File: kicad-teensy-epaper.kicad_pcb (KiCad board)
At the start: 2 copper layers, 78.8 x 57.3 mm, 21 parts, among them J1 TEENSY3.2-72MHz, J2 HEADER-FEMALE-34POS-FFC-SMT-1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, Q1 Q_NMOS_GDS

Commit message: label cap touch buttons
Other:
- board text added: "A"
- board text added: "B"
- board text added: "C"
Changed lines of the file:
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@@
     (area 64.696768 31.999281 143.613621 89.405461)
     (thickness 1.6)
-    (drawings 47)
+    (drawings 50)
     (tracks 198)
     (zones 0)
@@
       (net 55 "Net-(CAP3-Pad1)") (clearance 0.508))
   )
+  (gr_text "C\n" (at 135.24812 78.84616 90) (layer B.SilkS)
+    (effects (font (size 3 3) (thickness 0.4)) (justify mirror))
+  )
+  (gr_text "B\n" (at 135.06812 63.68616 90) (layer B.SilkS)
+    (effects (font (size 3 3) (thickness 0.4)) (justify mirror))
+  )
+  (gr_text A (at 134.77812 48.56616 90) (layer B.SilkS)
+    (effects (font (size 3 3) (thickness 0.4)) (justify mirror))
+  )
   (gr_text https://github.com/pdp7/kicad-teensy-epaper (at 103.54812 87.56616) (layer B.SilkS)

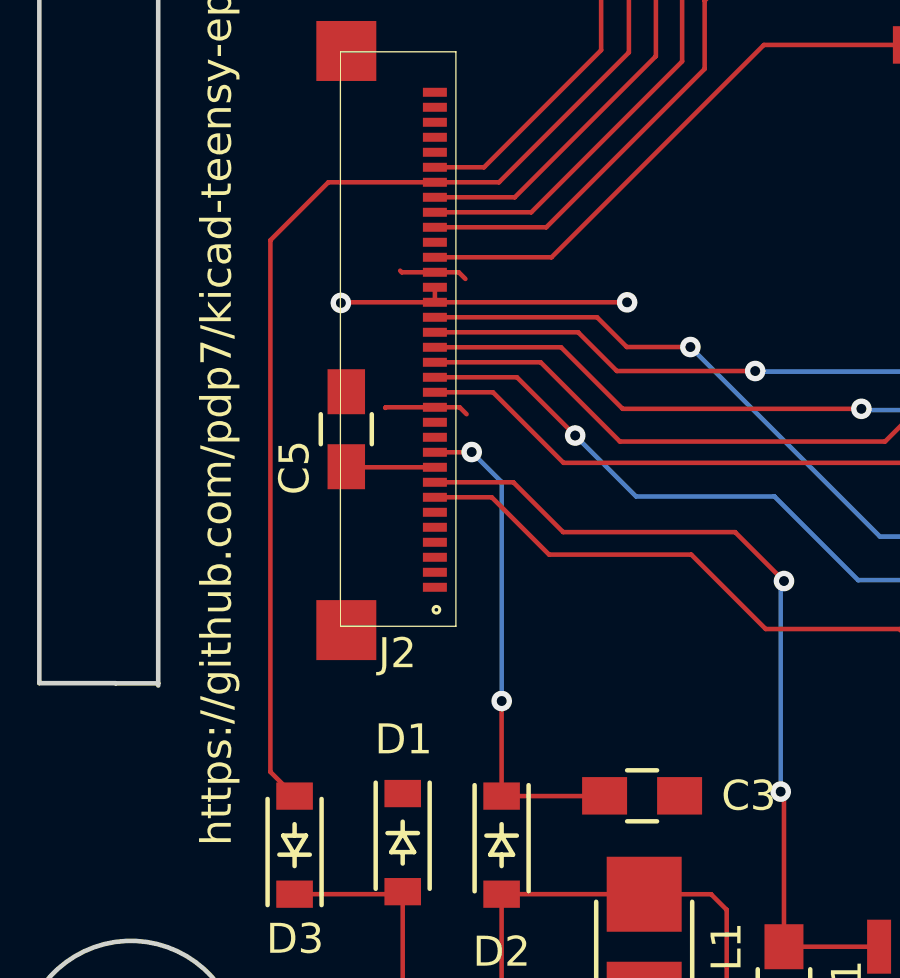
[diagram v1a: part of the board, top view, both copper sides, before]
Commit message: move C5 to avoid connector
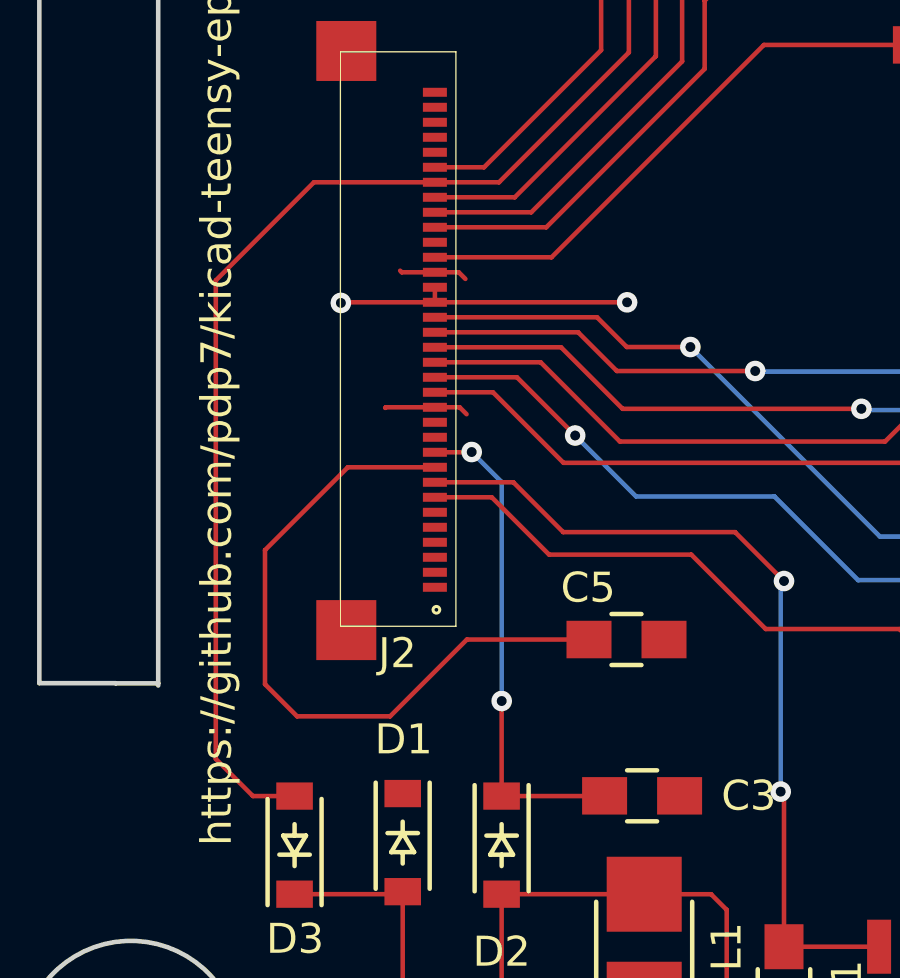
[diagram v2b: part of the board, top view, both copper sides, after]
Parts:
- moved C5 11.7 mm to (86.4, 70.6), turned to 180 degrees
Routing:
- net VGL: track 2.96 -> 23.6 mm
- net PRVGL: track 53.0 -> 55.6 mm
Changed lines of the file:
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@@
     (links 48)
     (no_connects 1)
-    (area 64.696768 31.999281 143.613621 89.405461)
+    (area 64.696768 31.999281 178.510001 123.265001)
     (thickness 1.6)
     (drawings 50)
-    (tracks 198)
+    (tracks 204)
     (zones 0)
     (modules 21)
@@
   )
   (module Capacitors_SMD:C_0805_HandSoldering (layer F.Cu)
-    (at 77.07812 63.58616 270)
+    (at 86.41812 70.59616 180)
     (descr "Capacitor SMD 0805, hand soldering")
     (tags "capacitor 0805")
     (attr smd)
-    (fp_text reference C5 (at 1.278 1.726 270) (layer F.SilkS)
-      (effects (font (size 1 1) (thickness 0.15)))
-    )
-    (fp_text value CAP-CER-1UF (at 0 2.1 270) (layer F.Fab)
+    (fp_text reference C5 (at 1.278 1.726 180) (layer F.SilkS)
+      (effects (font (size 1 1) (thickness 0.15)))
+    )
+    (fp_text value CAP-CER-1UF (at 0 2.1 180) (layer F.Fab)
       (effects (font (size 1 1) (thickness 0.15)))
     )
@@
     (fp_line (start 0.5 -0.85) (end -0.5 -0.85) (layer F.SilkS) (width 0.15))
     (fp_line (start -0.5 0.85) (end 0.5 0.85) (layer F.SilkS) (width 0.15))
-    (pad 1 smd rect (at -1.25 0 270) (size 1.5 1.25) (layers F.Cu F.Paste F.Mask)
-      (net 39 GND))
-    (pad 2 smd rect (at 1.25 0 270) (size 1.5 1.25) (layers F.Cu F.Paste F.Mask)
+    (pad 1 smd rect (at -1.25 0 180) (size 1.5 1.25) (layers F.Cu F.Paste F.Mask)
+      (net 39 GND))
+    (pad 2 smd rect (at 1.25 0 180) (size 1.5 1.25) (layers F.Cu F.Paste F.Mask)
       (net 20 VGL))
     (model Capacitors_SMD.3dshapes/C_0805_HandSoldering.wrl
@@
   (segment (start 82.25536 75.81468) (end 85.6796 75.81468) (width 0.1524) (layer F.Cu) (net 18))
   (segment (start 85.6796 75.81468) (end 85.68812 75.80616) (width 0.1524) (layer F.Cu) (net 18))
-  (segment (start 80.03184 55.3548) (end 76.47948 55.3548) (width 0.1524) (layer F.Cu) (net 19))
-  (segment (start 74.54812 75.00862) (end 75.35418 75.81468) (width 0.1524) (layer F.Cu) (net 19))
-  (segment (start 74.54812 57.28616) (end 74.54812 75.00862) (width 0.1524) (layer F.Cu) (net 19))
-  (segment (start 76.47948 55.3548) (end 74.54812 57.28616) (width 0.1524) (layer F.Cu) (net 19))
+  (segment (start 75.35418 75.81468) (end 73.96664 75.81468) (width 0.1524) (layer F.Cu) (net 19) (status 400000))
+  (segment (start 75.99948 55.3548) (end 80.03184 55.3548) (width 0.1524) (layer F.Cu) (net 19) (status 800000))
+  (segment (start 72.72812 58.62616) (end 75.99948 55.3548) (width 0.1524) (layer F.Cu) (net 19))
+  (segment (start 72.72812 74.57616) (end 72.72812 58.62616) (width 0.1524) (layer F.Cu) (net 19))
+  (segment (start 73.96664 75.81468) (end 72.72812 74.57616) (width 0.1524) (layer F.Cu) (net 19))
   (segment (start 80.03184 55.3548) (end 82.16948 55.3548) (width 0.1524) (layer F.Cu) (net 19))
   (segment (start 91.39812 38.12616) (end 96.04812 38.12616) (width 0.1524) (layer F.Cu) (net 19))
@@
   (segment (start 86.49812 51.02616) (end 86.49812 43.02616) (width 0.1524) (layer F.Cu) (net 19))
   (segment (start 82.16948 55.3548) (end 86.49812 51.02616) (width 0.1524) (layer F.Cu) (net 19))
-  (segment (start 80.03184 64.8548) (end 77.09676 64.8548) (width 0.1524) (layer F.Cu) (net 20))
-  (segment (start 77.09676 64.8548) (end 77.07812 64.83616) (width 0.1524) (layer F.Cu) (net 20))
+  (segment (start 80.03184 64.8548) (end 77.12948 64.8548) (width 0.1524) (layer F.Cu) (net 20) (status 400000))
+  (segment (start 81.09812 70.59616) (end 85.16812 70.59616) (width 0.1524) (layer F.Cu) (net 20) (status 800000))
+  (segment (start 78.53812 73.15616) (end 81.09812 70.59616) (width 0.1524) (layer F.Cu) (net 20))
+  (segment (start 75.43812 73.15616) (end 78.53812 73.15616) (width 0.1524) (layer F.Cu) (net 20))
+  (segment (start 74.36812 72.08616) (end 75.43812 73.15616) (width 0.1524) (layer F.Cu) (net 20))
+  (segment (start 74.36812 67.61616) (end 74.36812 72.08616) (width 0.1524) (layer F.Cu) (net 20))
+  (segment (start 77.12948 64.8548) (end 74.36812 67.61616) (width 0.1524) (layer F.Cu) (net 20))
   (segment (start 80.03184 57.8548) (end 83.91948 57.8548) (width 0.1524) (layer F.Cu) (net 21))
   (segment (start 90.99812 50.77616) (end 96.04812 50.77616) (width 0.1524) (layer F.Cu) (net 21))
